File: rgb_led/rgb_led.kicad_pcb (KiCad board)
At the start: 2 copper layers, 53.8 x 29.8 mm, 16 parts, among them SW1 SW_DPDT_x2

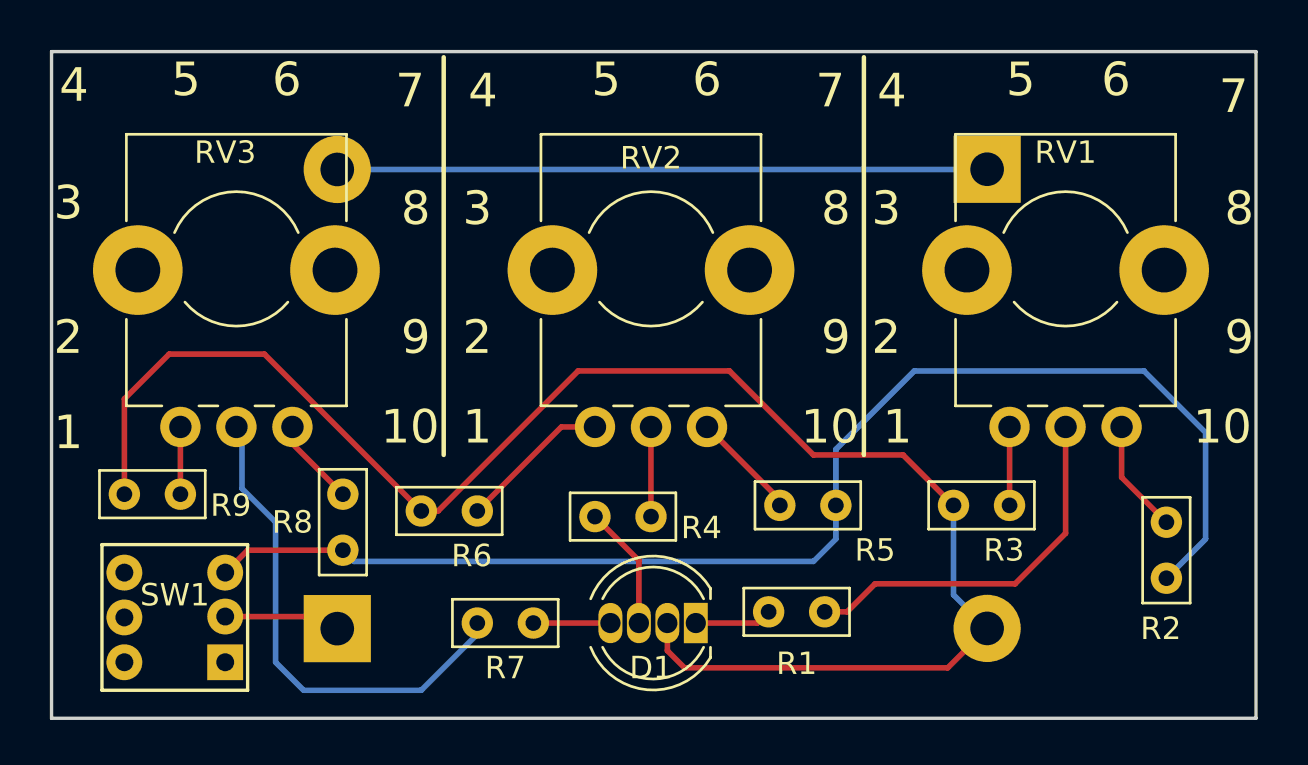
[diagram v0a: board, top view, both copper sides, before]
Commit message: RGB LED minor PCB changes
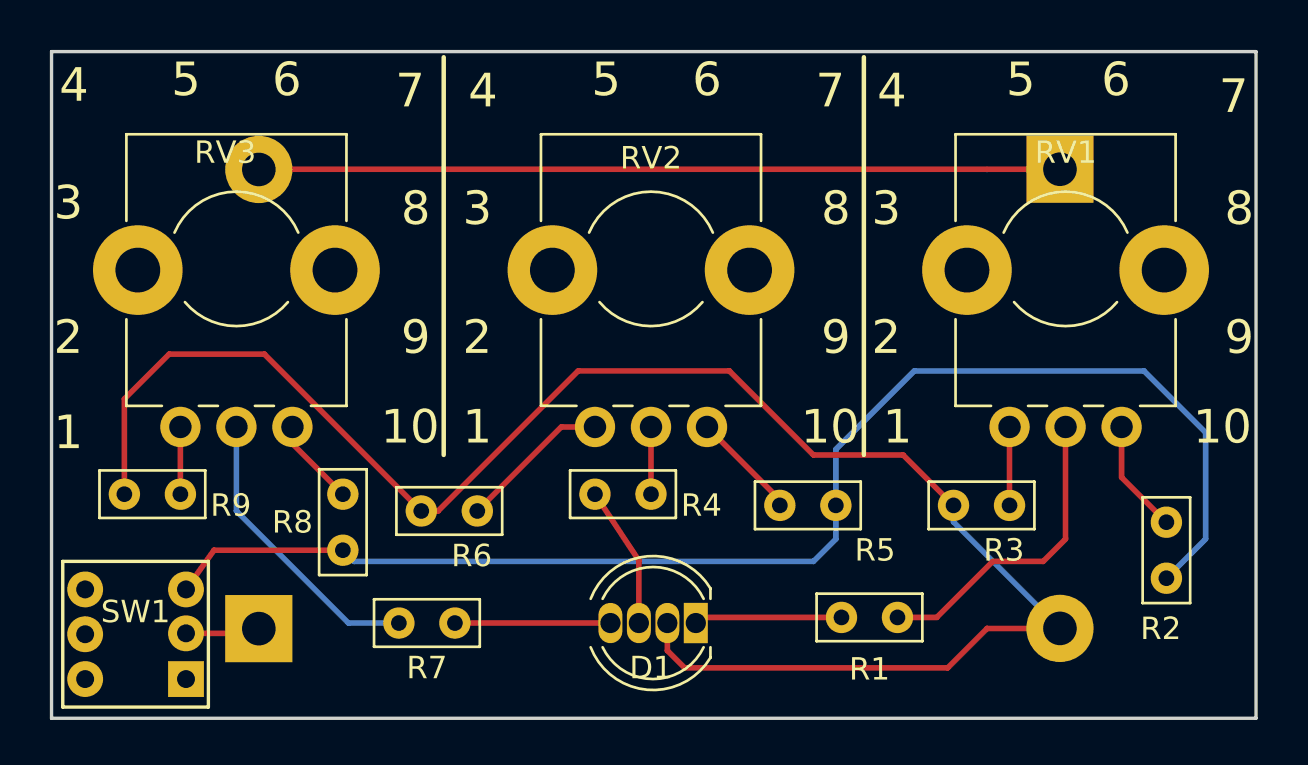
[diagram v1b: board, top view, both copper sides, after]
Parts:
- moved BT1 3.50 mm to (117.5, 118.5)
- moved R7 3.50 mm to (123.8, 118.2)
- moved R1 3.26 mm to (146.0, 118.0)
- moved BT2 3.25 mm to (153.2, 98.0)
- moved SW1 1.90 mm to (114.2, 120.8)
- moved R4 1.00 mm to (135.0, 112.5)
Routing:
- net Net-(R7-Pad1): track 22.3 -> 13.4 mm
- net Net-(BT1-Pad2): track 29.0 -> 35.8 mm
- net Net-(BT2-Pad2): track 72.7 -> 77.3 mm
- net Net-(D1-Pad4): track 3.44 -> 6.94 mm
- net Net-(D1-Pad1): track 3.46 -> 6.60 mm
- net Net-(R1-Pad1): track 16.9 -> 13.9 mm
- net Net-(R2-Pad1): track 58.6 -> 60.8 mm
- net Net-(BT1-Pad1): track 5.22 -> 3.34 mm
- net Net-(R4-Pad1): track 4.00 -> 3.00 mm
- net Net-(D1-Pad3): track 5.56 -> 6.34 mm
